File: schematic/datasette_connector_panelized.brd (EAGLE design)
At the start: 49.2 x 36.1 mm, 12 parts, among them CN1 C64_CASETTE_EDGE, CN11 C64_CASETTE_EDGE, CN12 C64_CASETTE_EDGE, CN13 C64_CASETTE_EDGE, CN3 C64_CASETTE_CONN, CN31 C64_CASETTE_CONN, CN32 C64_CASETTE_CONN, CN33 C64_CASETTE_CONN

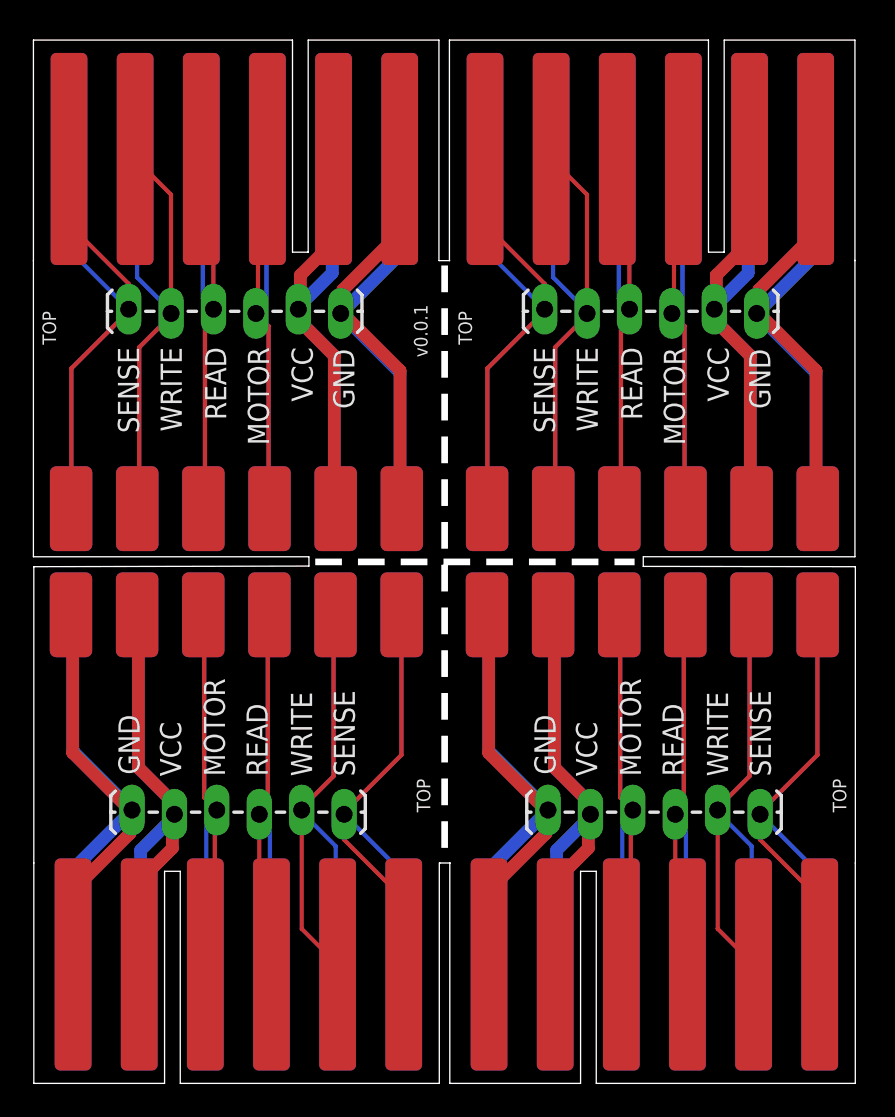
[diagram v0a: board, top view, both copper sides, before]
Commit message: laytout: datasette connect panelized fixes
gap has 1mm instead of 0.6mm since Seeed Studio doesn't support it
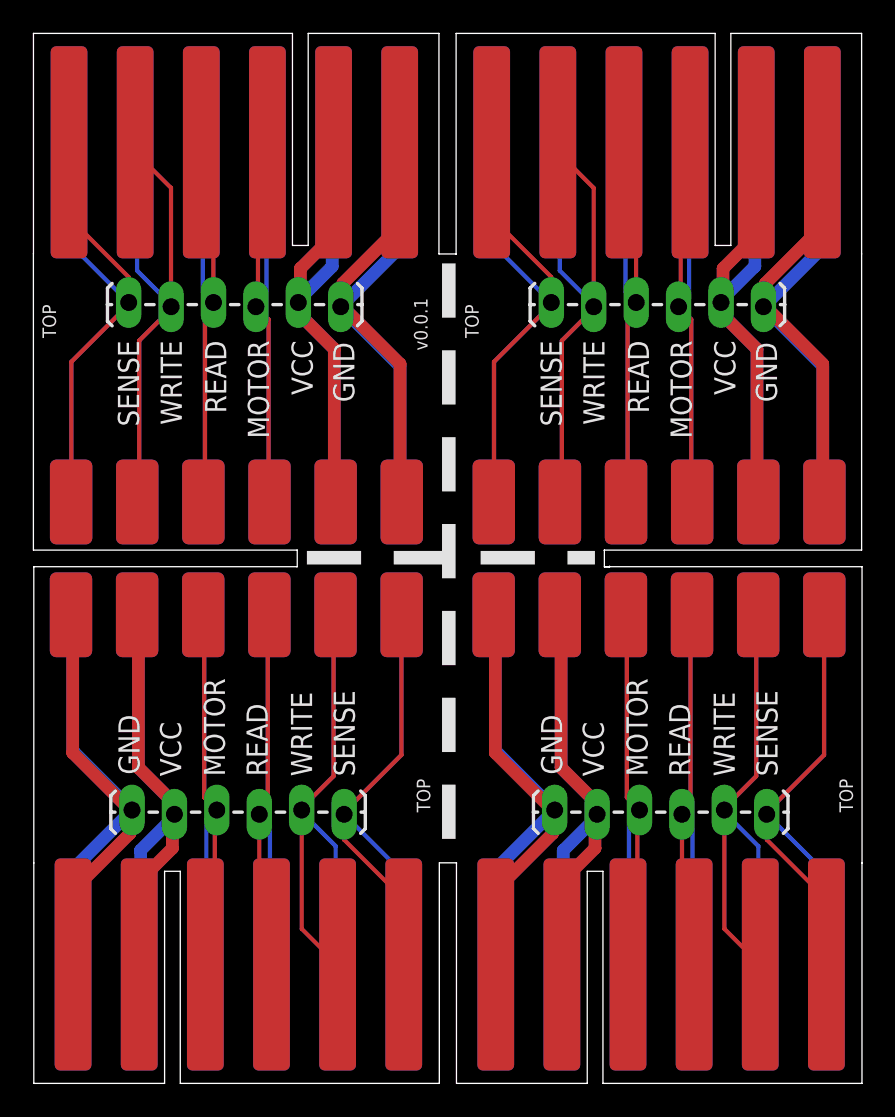
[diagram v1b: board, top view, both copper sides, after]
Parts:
- moved CN11 0.57 mm to (25.5, 55.3)
- moved JP1 0.57 mm to (43.7, 46.5)
- moved CN31 0.57 mm to (25.6, 31.2)
- moved CN1 0.40 mm to (0.15, 55.3)
- moved CN13 0.40 mm to (49.5, 7.64)
- moved CN33 0.40 mm to (49.3, 31.8)
- moved CN3 0.40 mm to (0.28, 31.2)
- moved JP 0.40 mm to (18.4, 46.5)
- moved JP3 0.40 mm to (31.2, 16.4)
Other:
- board size 49.2 x 36.1 mm -> 49.6 x 36.5 mm
